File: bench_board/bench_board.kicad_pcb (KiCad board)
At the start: 4 copper layers, 80 x 60 mm, 67 parts, among them J1 BATT_4S, J10 BUZZER, J2 BOOT0_JUMPER, J3 USB-C, J4 CRSF_UART, J5 DSHOT_M1-M4, J6 SWD, J7 RX_PWR_5V, J8 TELEM_TX, J9 EXPANSION_BUS, Q1 AO3400A, U1 STM32F405RGT6, U2 TPS54336ADDA, U4 MPU-6000, U5 USBLC6-2SC6, U6 MT3608, Y1 8MHz

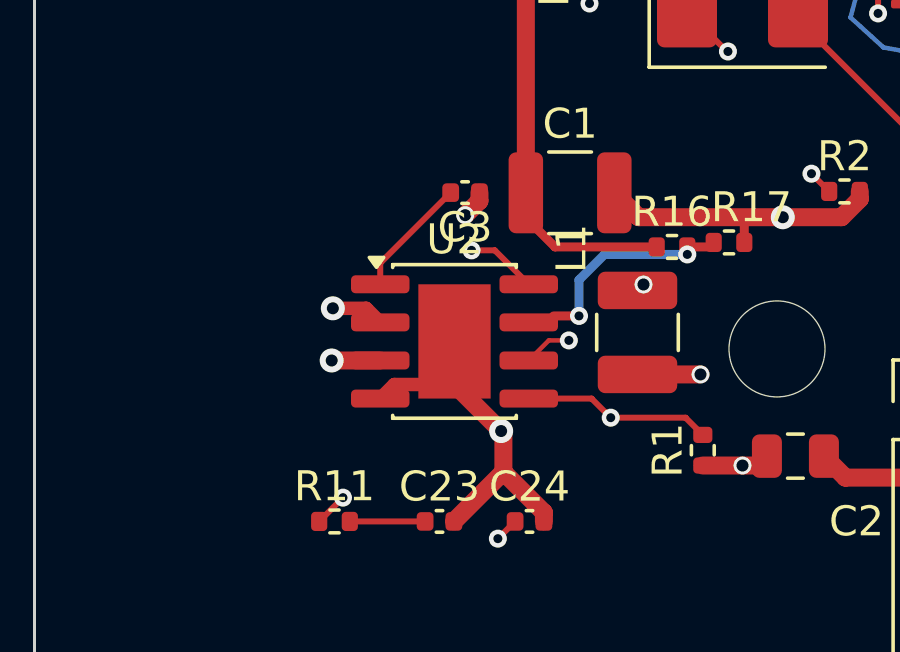
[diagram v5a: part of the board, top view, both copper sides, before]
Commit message: SW_NODE fixed properly: 16.16mm/3-via plane-slicer -> 4.79mm all-F.Cu
The buck's switch node ran 7 segments, 3 vias, 16.16mm, with 13.58mm
inside the In1 GND and In2 3V3 planes, because U2 pin 3 (PH) faces west
while L1 sat east. Now: L1 moved west of U2 (7.85,45.90, SW pad facing
pin 3), net is 3 segments, 4.79mm, 0 vias, 0.6mm width, F.Cu only.

Deliberate scope deviation, declared: C3 (bootstrap cap, pad 1 IS
/SW_NODE) relocated west to (8.30,43.00) with its /VBST_NODE stub
rerouted (4.0mm -> 2.75mm). Without moving C3 the <8mm criterion is
geometrically unreachable: U2's west pocket is walled by the pin
column (0.67mm gaps vs 1.0mm needed for a 0.6mm trace), the VBST
diagonal, and the VBAT_4S trace/via; any around-the-outside path to
C3.1 measures >=14mm. The brief's fallback (rotate U2 180, 7 nets
disturbed) is strictly worse. Input loop (C1/VBAT via) untouched.

3V3 output: old L1.2 stub+via at (22.20,46.10) deleted; new 0.95mm
trace + via (5.50,45.90) into the In2 3V3 plane.

Measured, not asserted:
- inner-layer /SW_NODE segments: 0 (was 4)
- total length 4.790mm (was 16.16), all width 0.6mm, 0 vias
- guard PASS+ 51/2/95, ratcheted from 53/2/95 (the -2 = L1's old
  RefDes silk overlaps, gone with the move); DRC diff vs baseline
  shows ZERO new violations
- ERC 0 before and after; zone refill coherent (4 -> 4 polygons/plane)
- falsifiability audit 18/18 exit 0

Pre-commit verifier: HOLD-FIX-FIRST -> fixed (stale _guard_drc.json
from the falsifiability audit's mutated-board run; reconciled with a
fresh guard PASS). Undo: git revert this commit; the guard baseline
ratchet then needs board_guard.py baseline re-run at HEAD~1.

Co-Authored-By: Claude Fable 5 <noreply@anthropic.com>
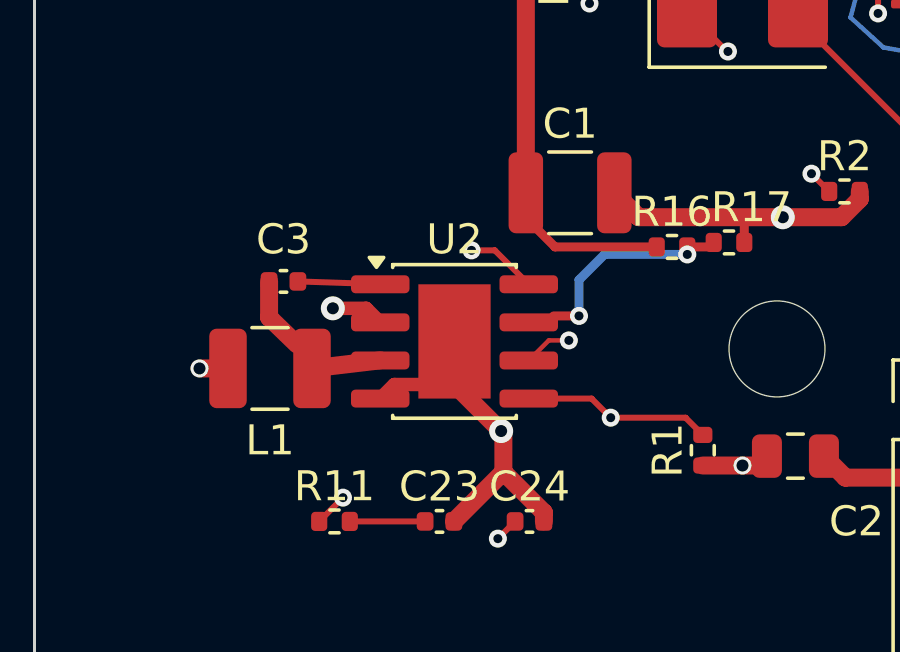
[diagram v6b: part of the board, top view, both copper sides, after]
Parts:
- moved L1 12.3 mm to (7.85, 45.9), turned to 180 degrees
- moved C3 6.74 mm to (8.30, 43.0), turned to 0 degrees
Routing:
- net /SW_NODE: track 16.2 -> 4.79 mm, vias 3 -> 0
- net /VBST_NODE: track 4.03 -> 2.75 mm
- net /3V3: track 55.3 -> 54.2 mm
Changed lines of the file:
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@@
 	(footprint "Inductor_SMD:L_1210_3225Metric"
 		(layer "F.Cu")
-		(at 20.1 44.7 -90)
+		(at 7.85 45.9 180)
 		(descr "Inductor SMD 1210 (3225 Metric), square (rectangular) end terminal, IPC-7351 nominal, (Body size source: http://www.tortai-tech.com/upload/download/2011102023233369053.pdf)")
 		(tags "inductor")
 		(property "Reference" "L1"
-			(at -2.8 2.2 270)
+			(at 0 -2.4 180)
 			(layer "F.SilkS")
 			(effects
@@
 		)
 		(property "Value" "10uH"
-			(at 0 2.28 270)
+			(at 0 2.28 180)
 			(layer "F.Fab")
 			(effects
@@
 		)
 		(property "Datasheet" ""
-			(at 0 0 270)
+			(at 0 0 180)
 			(layer "F.Fab")
 			(hide yes)
@@
 		)
 		(property "Description" ""
-			(at 0 0 270)
+			(at 0 0 180)
 			(layer "F.Fab")
 			(hide yes)
@@
 		)
 		(property "KiLib_Generator" "SMD_2terminal_chip_molded"
-			(at 0 0 270)
+			(at 0 0 180)
 			(layer "F.SilkS")
 			(hide yes)
@@
 		)
 		(fp_text user "${REFERENCE}"
-			(at 0 0 270)
+			(at 0 0 180)
 			(layer "F.Fab")
 			(effects
@@
 		)
 		(pad "1" smd roundrect
-			(at -1.4 0 270)
+			(at -1.4 0 180)
 			(size 1.25 2.65)
 			(layers "F.Cu" "F.Mask" "F.Paste")
@@
 		)
 		(pad "2" smd roundrect
-			(at 1.4 0 270)
+			(at 1.4 0 180)
 			(size 1.25 2.65)
 			(layers "F.Cu" "F.Mask" "F.Paste")
@@
 	(footprint "Capacitor_SMD:C_0402_1005Metric"
 		(layer "F.Cu")
-		(at 14.352 40.039 180)
+		(at 8.3 43)
 		(descr "Capacitor SMD 0402 (1005 Metric), square (rectangular) end terminal, IPC-7351 nominal, (Body size source: IPC-SM-782 page 76, https://www.pcb-3d.com/wordpress/wp-content/uploads/ipc-sm-782a_amendment_1_and_2.pdf)")
 		(tags "capacitor")
 		(property "Reference" "C3"
-			(at 0 -1.16 180)
+			(at 0 -1.4 0)
 			(layer "F.SilkS")
 			(effects
@@
 		)
 		(property "Value" "100nF"
-			(at 0 1.16 180)
+			(at 0 1.16 0)
 			(layer "F.Fab")
 			(effects
@@
 		)
 		(property "Datasheet" ""
-			(at 0 0 180)
+			(at 0 0 0)
 			(layer "F.Fab")
 			(hide yes)
@@
 		)
 		(property "Description" ""
-			(at 0 0 180)
+			(at 0 0 0)
 			(layer "F.Fab")
 			(hide yes)
@@
 		)
 		(property "KiLib_Generator" "SMD_2terminal_chip_molded"
-			(at 0 0 180)
+			(at 0 0 0)
 			(layer "F.SilkS")
 			(hide yes)
@@
 		(duplicate_pad_numbers_are_jumpers no)
 		(fp_line
-			(start -0.107836 0.36)
-			(end 0.107836 0.36)
+			(start -0.107836 -0.36)
+			(end 0.107836 -0.36)
 			(stroke
 				(width 0.12)
@@
 		)
 		(fp_line
-			(start -0.107836 -0.36)
-			(end 0.107836 -0.36)
+			(start -0.107836 0.36)
+			(end 0.107836 0.36)
 			(stroke
 				(width 0.12)
@@
 		)
 		(fp_text user "${REFERENCE}"
-			(at 0 0 180)
+			(at 0 0 0)
 			(layer "F.Fab")
 			(effects
@@
 		)
 		(pad "1" smd roundrect
-			(at -0.48 0 180)
+			(at -0.48 0)
 			(size 0.56 0.62)
 			(layers "F.Cu" "F.Mask" "F.Paste")
@@
 		)
 		(pad "2" smd roundrect
-			(at 0.48 0 180)
+			(at 0.48 0)
 			(size 0.56 0.62)
 			(layers "F.Cu" "F.Mask" "F.Paste")
@@
 	)
 	(segment
-		(start 20.1 46.1)
-		(end 22.2 46.1)
-		(width 0.6)
-		(layer "F.Cu")
-		(net "/3V3")
-	)
-	(segment
 		(start 31.25 25.1)
 		(end 30.1 26.25)
@@
 	)
 	(segment
+		(start 6.45 45.9)
+		(end 5.5 45.9)
+		(width 0.6)
+		(layer "F.Cu")
+		(net "/3V3")
+	)
+	(segment
 		(start 36.985 39.819)
 		(end 37.9761 38.8279)
@@
 	)
 	(via
-		(at 22.2 46.1)
-		(size 0.6)
-		(drill 0.4)
-		(layers "F.Cu" "B.Cu")
-		(net "/3V3")
-	)
-	(via
 		(at 13.2738 6.1033)
 		(size 0.6)
@@
 	)
 	(via
+		(at 5.5 45.9)
+		(size 0.6)
+		(drill 0.4)
+		(layers "F.Cu" "B.Cu")
+		(net "/3V3")
+	)
+	(via
 		(at 23.6 49.136)
 		(size 0.6)
@@
 	)
 	(segment
+		(start 45.095 32.187)
+		(end 45.75 32.187)
+		(width 0.3)
+		(layer "F.Cu")
+		(net "/GND")
+	)
+	(segment
 		(start 63.7133 24.1492)
 		(end 63.8625 24)
@@
 	)
 	(segment
+		(start 45.75 32.187)
+		(end 46.35 31.587)
+		(width 0.3)
+		(layer "F.Cu")
+		(net "/GND")
+	)
+	(segment
 		(start 17.5169 27.7193)
 		(end 18.4219 27.7193)
@@
 	)
 	(segment
+		(start 46.35 31.587)
+		(end 46.35 30.049)
+		(width 0.3)
+		(layer "F.Cu")
+		(net "/GND")
+	)
+	(segment
 		(start 39.047 41.899)
 		(end 40.7407 43.5927)
@@
 	)
 	(segment
-		(start 13.872 40.039)
-		(end 11.525 42.386)
+		(start 8.78 43)
+		(end 11.53 43.09)
 		(width 0.2)
 		(layer "F.Cu")
@@
 	)
 	(segment
-		(start 11.525 42.386)
-		(end 11.525 43.095)
-		(width 0.2)
-		(layer "F.Cu")
-		(net "/VBST_NODE")
-	)
-	(segment
-		(start 14.832 40.3153)
-		(end 14.832 40.039)
+		(start 7.82 43)
+		(end 7.82 44.2)
 		(width 0.6)
 		(layer "F.Cu")
@@
 	)
 	(segment
-		(start 11.525 45.635)
-		(end 9.9056 45.635)
+		(start 11.53 45.63)
+		(end 9.25 45.9)
 		(width 0.6)
 		(layer "F.Cu")
@@
 	)
 	(segment
-		(start 14.3565 40.7908)
-		(end 14.832 40.3153)
+		(start 7.82 44.2)
+		(end 8.75 45.1)
 		(width 0.6)
 		(layer "F.Cu")
 		(net "/SW_NODE")
 	)
-	(via
-		(at 14.3565 40.7908)
-		(size 0.6)
-		(drill 0.4)
-		(layers "F.Cu" "B.Cu")
-		(net "/SW_NODE")
-	)
-	(via
-		(at 9.9056 45.635)
-		(size 0.8)
-		(drill 0.4)
-		(layers "F.Cu" "B.Cu")
-		(net "/SW_NODE")
-	)
-	(via
-		(at 20.3 43.1025)
-		(size 0.6)
-		(drill 0.4)
-		(layers "F.Cu" "B.Cu")
-		(net "/SW_NODE")
-	)
-	(segment
-		(start 9.9056 45.635)
-		(end 9.9056 45.2417)
-		(width 0.6)
-		(layer "In1.Cu")
-		(net "/SW_NODE")
-	)
-	(segment
-		(start 9.9056 45.2417)
-		(end 14.3565 40.7908)
-		(width 0.6)
-		(layer "In1.Cu")
-		(net "/SW_NODE")
-	)
-	(segment
-		(start 17.9883 40.7908)
-		(end 20.3 43.1025)
-		(width 0.6)
-		(layer "In2.Cu")
-		(net "/SW_NODE")
-	)
-	(segment
-		(start 14.3565 40.7908)
-		(end 17.9883 40.7908)
-		(width 0.6)
-		(layer "In2.Cu")
-		(net "/SW_NODE")
-	)
 	(segment
 		(start 15.4461 51.5739)
@@
 		(net "/USB_DP_MCU")
 	)
-	(segment
-		(start 45.095 32.187)
-		(end 45.75 32.187)
-		(width 0.3)
-		(layer "F.Cu")
-		(net "/GND")
-	)
-	(segment
-		(start 45.75 32.187)
-		(end 46.35 31.587)
-		(width 0.3)
-		(layer "F.Cu")
-		(net "/GND")
-	)
-	(segment
-		(start 46.35 31.587)
-		(end 46.35 30.049)
-		(width 0.3)
-		(layer "F.Cu")
-		(net "/GND")
-	)
 	(zone

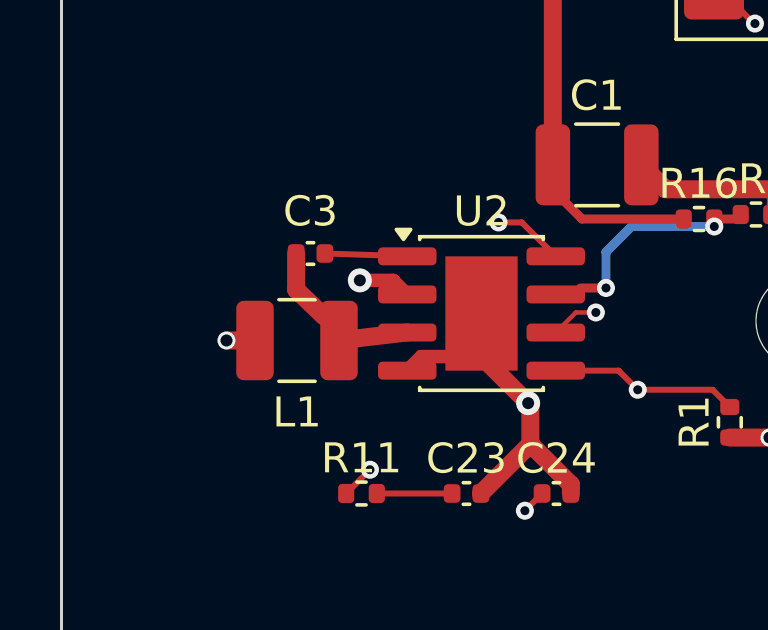
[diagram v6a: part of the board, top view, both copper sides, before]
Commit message: Review fixes: SW branch to L1.1 anchor; ERC-before evidence; ignore .history/
Independent batch review (fresh Opus agent, read-only) returned
0 BLOCKER / 1 HIGH / 2 MEDIUM / 6 LOW and independently confirmed all
five acceptance criteria, the guard hash chain, zero out-of-scope
copper deltas, and that the input loop measurably improved (In2 plane
under C1: 9.31 -> 13.50 mm2 solid after the SW slot's removal).

Acted on here:
- MEDIUM-2: the C3 bootstrap branch ended 0.125mm inside L1 pad 1's
  west edge; it now terminates at the pad anchor (9.25,45.90).
  /SW_NODE total is 5.717mm (still <8mm), guard PASS 51/2/95.
- LOW-2: the batch-start ERC run (0 violations, captured before any
  edit) is now committed as bench_board/erc_swnode_before.json.
- LOW-4: .history/ (editor local-history holding a full board copy)
  is now gitignored.

Corrections to the previous commit's message, for the record:
- The -2 ratchet was funded by BOTH moved RefDes fields (L1-vs-C1 and
  C3-vs-U2 silk overlaps), not L1's alone, and partly by the RefDes
  repositioning itself -- which was required to avoid NEW
  silk_over_copper violations at the moved locations (the 58-violation
  FAIL in the guard log), not opportunistic silk cleanup. Parts were
  moved, not re-instantiated (footprint UUIDs unchanged).
- The ">=14mm" around-the-outside figure assumed VBAT_4S's approach to
  U2 pin 2 stays west; the reviewer's ~11mm construct crosses the
  VBAT_4S trace at y=43.9 (x 9.715-11.285) and is blocked as drawn.
  Either number busts the 8mm budget; conclusion unchanged.

Not acted on, deliberately: HIGH-1 (C3//VBST_NODE scope deviation)
needs the batch owner's ratification -- reported in wiki/log.md and
FINAL-REPORT.md, with the revert path stated. LOW-3 (fab/2026-08-18a
CPL matches master, not this branch) is recorded in the report and
wiki/.next-prompt.txt rather than by editing the ordered package.

Co-Authored-By: Claude Fable 5 <noreply@anthropic.com>
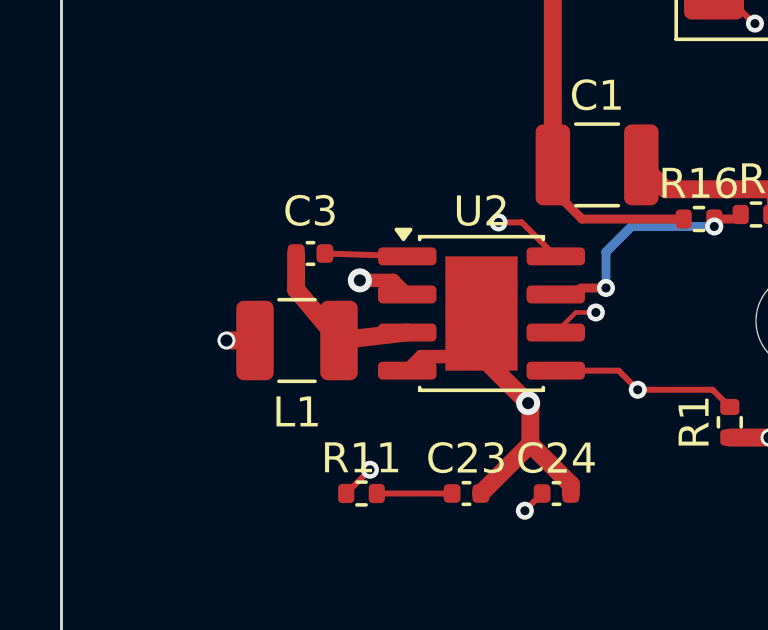
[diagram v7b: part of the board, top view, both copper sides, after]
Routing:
- net /SW_NODE: track 4.79 -> 5.72 mm
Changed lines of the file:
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@@
 	(segment
 		(start 7.82 44.2)
-		(end 8.75 45.1)
+		(end 9.25 45.9)
 		(width 0.6)
 		(layer "F.Cu")
